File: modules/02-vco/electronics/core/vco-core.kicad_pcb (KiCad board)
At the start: 2 copper layers, 58 x 110 mm, 146 parts, among them J1 Conn_01x04, J2 Conn_02x05_Odd_Even, J3 Conn_02x05_Odd_Even, J4 Conn_01x02, J5 Conn_02x03_Odd_Even, J6 Conn_02x02_Counter_Clockwise, J8 Conn_01x07, Q1 BC847BS, Q2 MMBT3906, Q3 J111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

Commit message: Fix: Replace generic MMBT3906 with ON Semi for Q2
Q2 is the actuator in the master current servo loop (U1B → Q2) that sets the tail current for the exponential converter. The previous BOM specified the generic LCSC part C7420354, which JLCPCB silently substituted between production batches: batch 1 (Jan 2026) received a working part, while batches 2 and 3 received Zhuhai Hongjiacheng (R+O) MMBT3906 parts under the same C-code.

The R+O datasheet only characterizes hFE at IC = −10 mA and above, with no minimum specified at low collector currents. The circuit operates Q2 at sub-milliamp currents, where the substituted part has insufficient gain to close the servo loop. U1B saturates against the negative supply rail trying to compensate, leaving Q2's collector current stuck at a fixed (too-low) value regardless of CV input.
Symptoms across all affected boards (20+ units, fully uniform):

- VCO pitch ceiling at ~70 Hz
- Pitch plateaus and flattens above a certain CV — no further response to increasing CV
- R_BIAS1 trim has no effect on output (loop railed)
- TP1 floats at ~1V instead of being servoed to 0V
- U1B output pinned at −10.3V (TL072 negative rail)

Verified by swapping Q2 with a verified-genuine 2N3906 on two broken boards — both immediately tracked V/oct correctly across full CV range.
The replacement part ON Semi MMBT3906LT1G (LCSC C53444) explicitly specifies hFE ≥ 60 at IC = −0.1 mA in its datasheet, guaranteeing correct behavior in this circuit's operating range.
Changes:

BOM: Q2 LCSC part number changed from C7420354 → C53444
Schematic annotation updated to specify ON Semi MMBT3906LT1G
Production note added: "Q2 (C53444): Do not substitute. Must be ON Semi MMBT3906LT1G."
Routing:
- net /Raw oscillator/I_REF: track 32.2 -> 31.6 mm
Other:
- board text added: "SHMØERGH MODULEUR VCO REV 3"
- board text added: "VCO Core REV 1"
- board text removed: "SHMØERGH MODULEUR VCO V1.0 2025 DEC"
- board text removed: "SM-02 Analog VCO Core V1.0 / 2025 Dec"

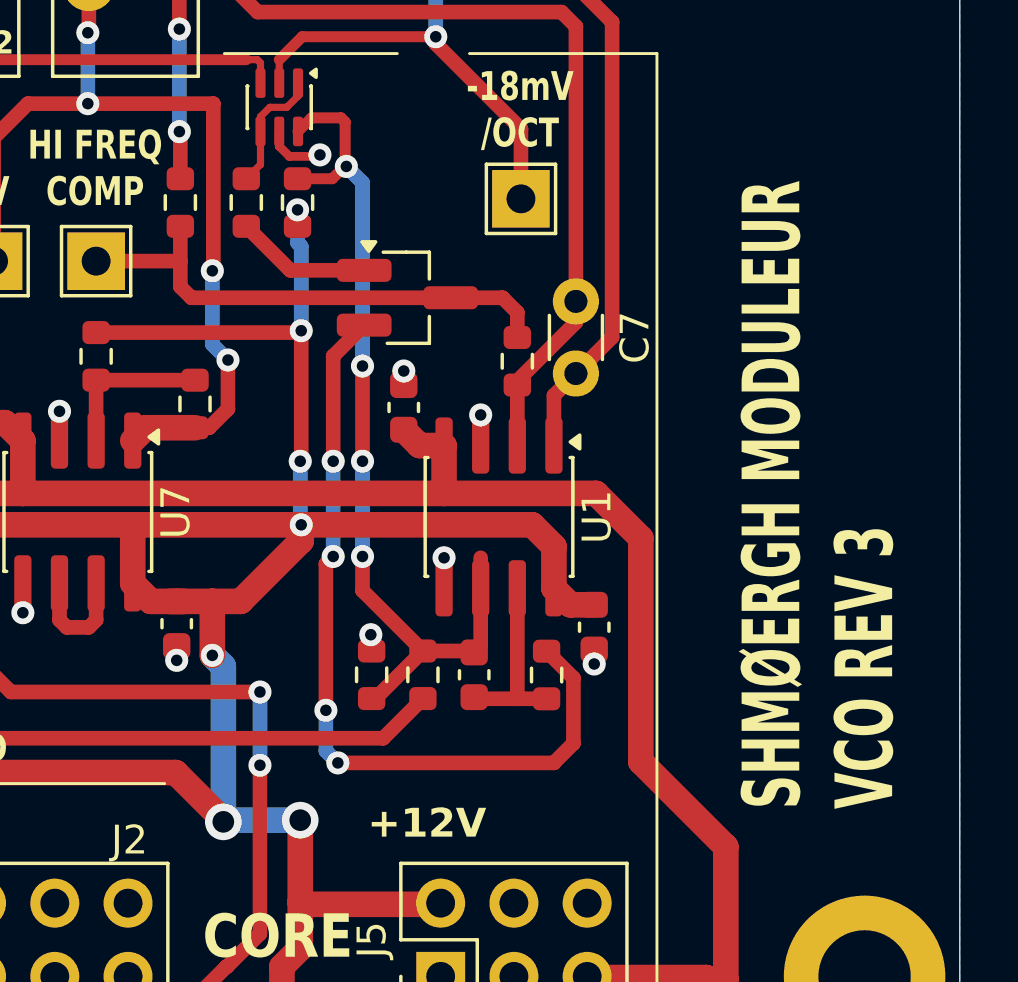
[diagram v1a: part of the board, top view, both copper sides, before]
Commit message: Fixed Q2 footprint pin numbering
Previous production used the SMD MMBT3906 with traces routed to the wrong pads, leaving the transistor operating in reverse-active mode. This barely worked with some manufacturer's parts and failed entirely with others (specifically Zhuhai Hongjiacheng R+O parts in batches 2 and 3), producing a uniform pitch ceiling at ~70 Hz across all affected units.

For further information and manual fix, refer to VCO FIXLOG in the modules folder.
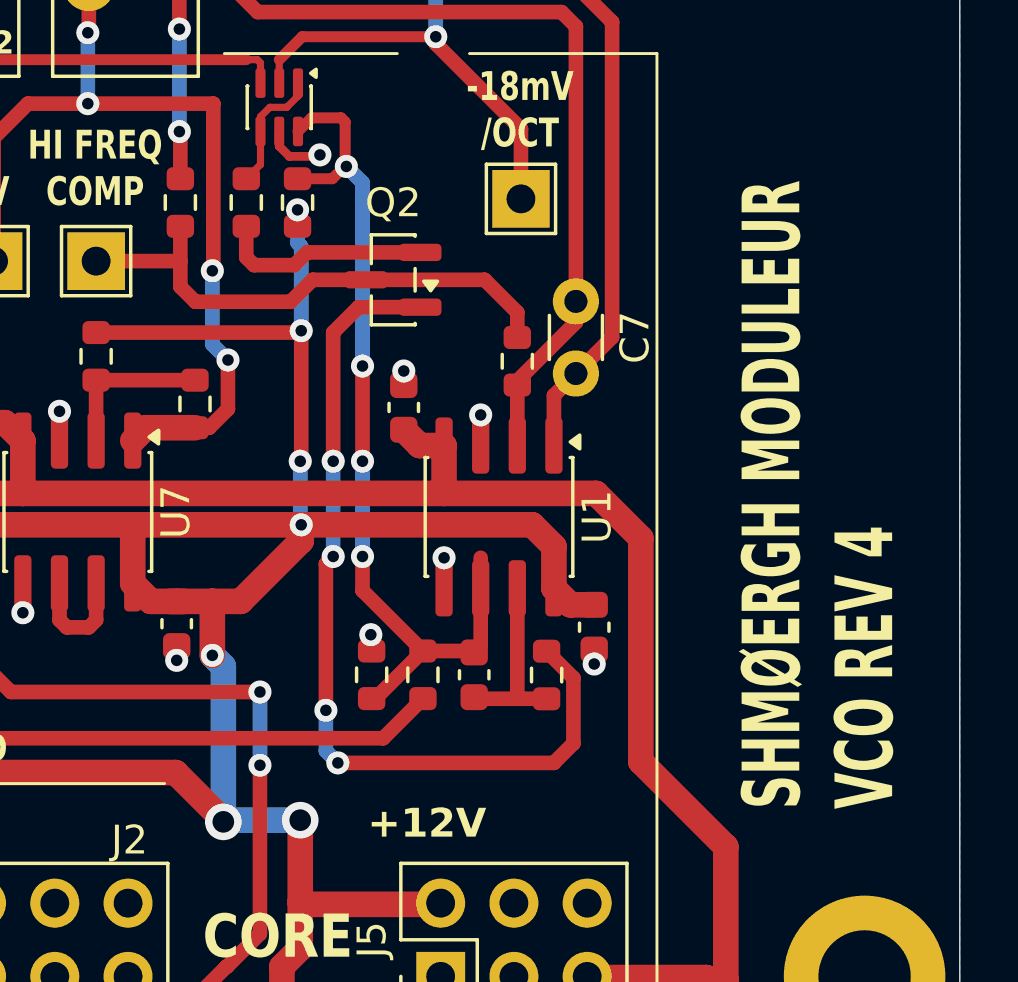
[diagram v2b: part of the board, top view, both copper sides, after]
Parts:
- Q2: footprint Package_TO_SOT_SMD:SOT-23_Handsoldering -> Package_TO_SOT_SMD:SOT-23
- moved Q2 0.79 mm to (162.4, 73.8), turned to 180 degrees
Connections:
- Q2 pad 1: Net-(Q2-E) -> Net-(Q2-B)
- Q2 pad 2: Net-(Q2-B) -> Net-(Q2-E)
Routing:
- net Net-(Q2-E): track 4.72 -> 7.40 mm
- net Net-(Q2-B): track 27.9 -> 30.6 mm
- net /Raw oscillator/HI_FREQ_COMP: track 17.9 -> 18.6 mm
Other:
- board text added: "SHMØERGH MODULEUR VCO REV 4"
- board text removed: "SHMØERGH MODULEUR VCO REV 3"
